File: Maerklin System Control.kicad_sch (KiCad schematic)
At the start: 20 parts, among them J1 Female Header, J2 Output, J3 Input, J4 Conn_S3 Mini, SW1 UP, SW2 RIGHT, SW3 DOWN, SW4 LEFT, SW5 SELECT, SW6 BACK

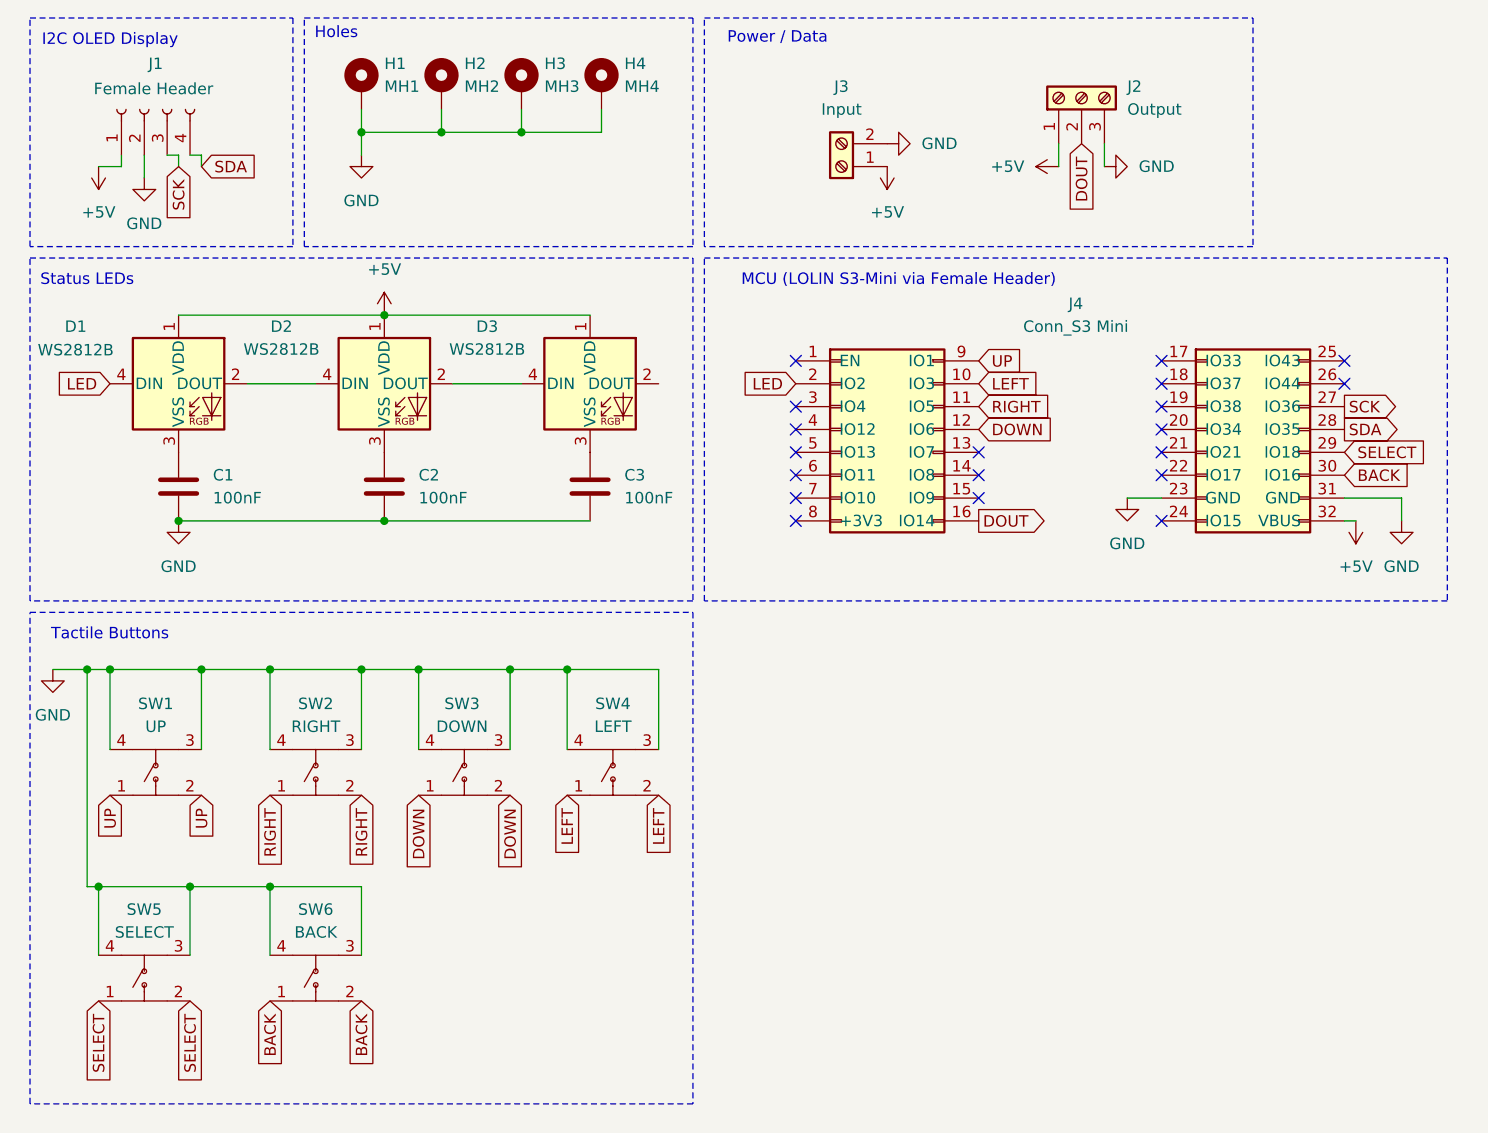
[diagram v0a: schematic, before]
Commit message: FIX: WLED connection
Signed-off-by: Peter Siegmund <mars3142@users.noreply.github.com>
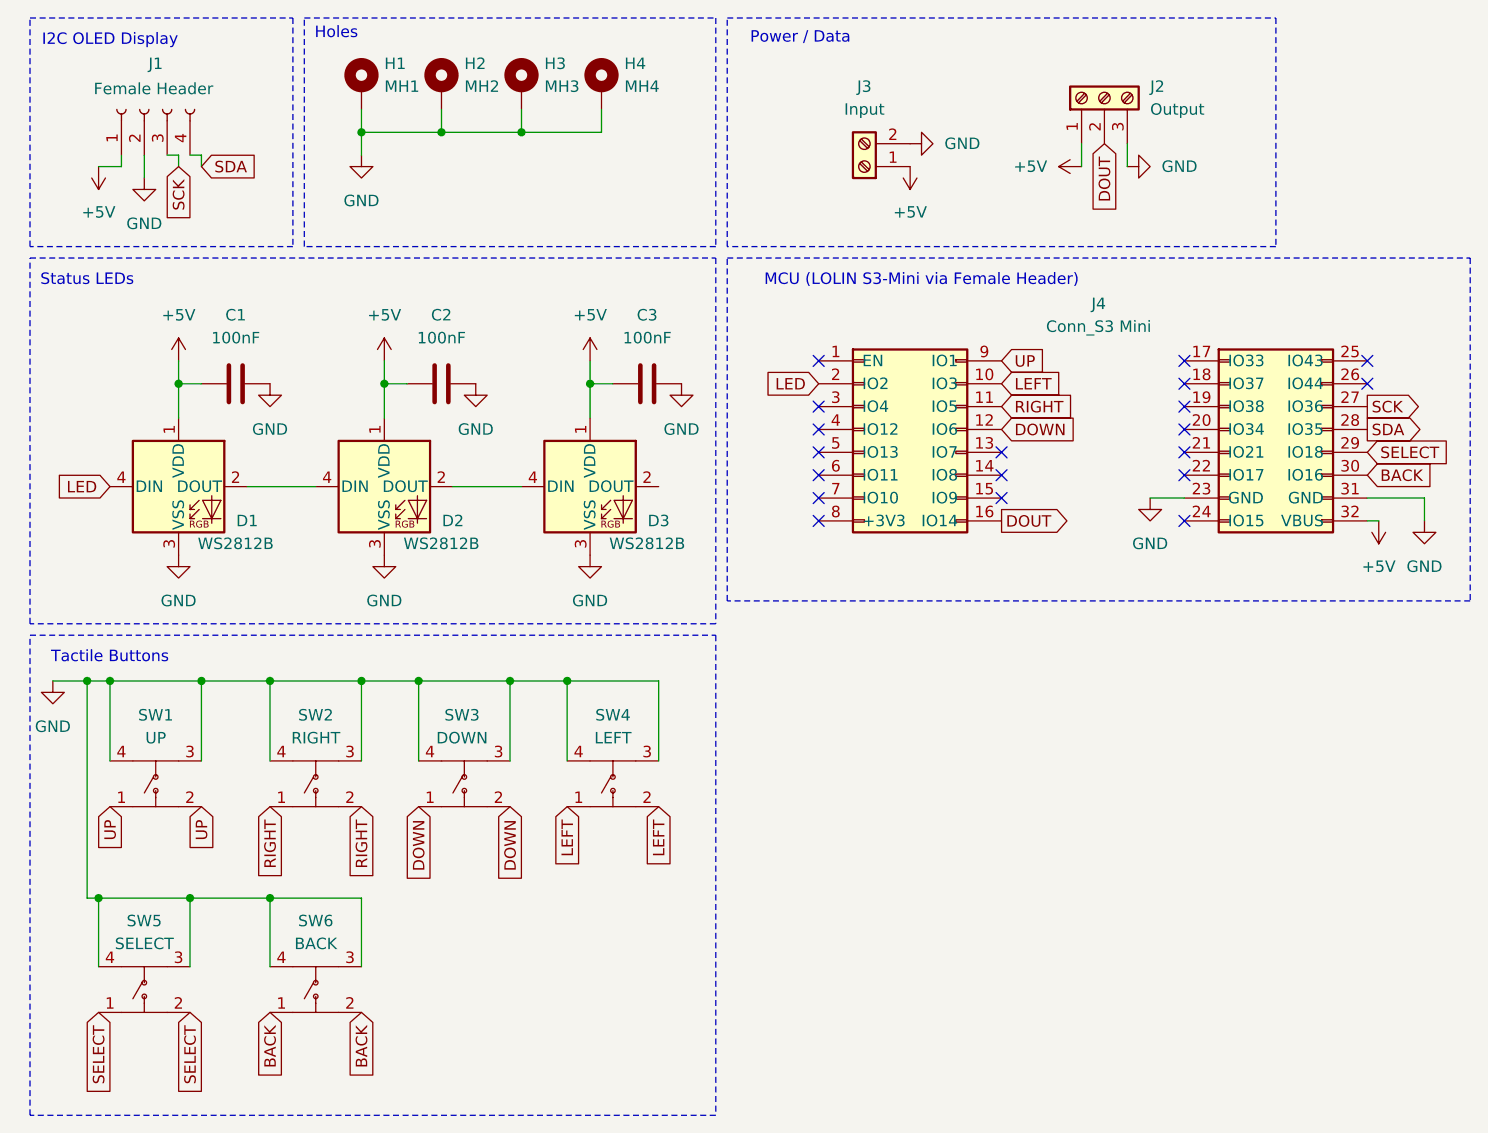
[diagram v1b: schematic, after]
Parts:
- C1, C2, C3: footprint Capacitor_SMD:C_0805_2012Metric -> Capacitor_SMD:C_0805_2012Metric_Pad1.18x1.45mm_HandSolder; LCSC (none) -> C1711
- D1, D2, D3: LCSC (none) -> C22371521
- J2: LCSC (none) -> C5188435
- J3: LCSC (none) -> C5188434
- J4: LCSC (none) -> C18722935
- SW1, SW2, SW3, SW5, SW6: LCSC (none) -> C83205
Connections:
- net +5V: now also C1.1, C2.1, C3.1
- net GND: now also D1.3 (VSS), D2.3 (VSS), D3.3 (VSS)
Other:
- moved on the sheet: C1, C2, C3, D1, D2, D3, J2, J3, J4, SW1, SW2, SW3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

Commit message: update sheet comments
Signed-off-by: Peter Siegmund <mars3142@users.noreply.github.com>
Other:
- company: mars3142 -> Peter Siegmund
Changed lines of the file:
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@@
 		(date "31.12.2025")
 		(rev "MK2.1")
-		(company "mars3142")
-		(comment 3 "System Control Board for model railway")
-		(comment 4 "Author: Peter Siegmund")
+		(company "Peter Siegmund")
+		(comment 1 "kicad@mars3142.org")
+		(comment 2 "https://wiki.mars3142.dev/project/maerklin/system_control/start")
 	)
 	(rectangle
